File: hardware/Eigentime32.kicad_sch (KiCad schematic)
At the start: 0 parts

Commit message: Add Power schematic sheet
CR2032 in a Keystone 3034 SMT retainer, DMG2305UX P-FET reverse
protection (gate to GND), 100 uF + 100 nF on VBAT, and a TPS61099
adjustable boost set to 3.0 V (R1 402k / R2 200k, 1 uH WE-LQS,
10 uF CIN, 2 x 10 uF COUT, 1M pull-down on EN). The sheet exposes
VBAT, VLCD and LCD_PWR_EN as hierarchical pins. ERC is clean with
all severities enabled.

Co-Authored-By: Claude Opus 5.5 (1M context) <noreply@anthropic.com>
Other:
- added sheet Power (power.kicad_sch)
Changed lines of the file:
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@@
 	(generator_version "9.0")
 	(paper "A4")
-	(title_block
-		(title "Eigentime32")
+	(title_block (title "Eigentime32"))
+	(sheet (at 50.8 50.8) (size 30.48 15.24) (exclude_from_sim no) (in_bom yes) (on_board yes) (dnp no)
+		(fields_autoplaced yes)
+		(stroke (width 0.1524) (type solid))
+		(fill (color 0 0 0 0.0000))
+		(property "Sheetname" "Power" (at 50.8 50.0884 0) (effects (font (size 1.27 1.27)) (justify left bottom)))
+		(property "Sheetfile" "power.kicad_sch" (at 50.8 66.6246 0) (effects (font (size 1.27 1.27)) (justify left top)))
+		(pin "VBAT" output (at 81.28 53.34 0) (effects (font (size 1.27 1.27)) (justify right)))
+		(pin "VLCD" output (at 81.28 55.88 0) (effects (font (size 1.27 1.27)) (justify right)))
+		(pin "LCD_PWR_EN" input (at 81.28 58.42 0) (effects (font (size 1.27 1.27)) (justify right)))
+		(instances (project "Eigentime32" (path "/6b2f6c1e-3a0d-4e6b-9a51-0e5c2f3d7a10" (page "2"))))
 	)
-	(sheet_instances
-		(path "/"
-			(page "1")
-		)
-	)
+	(wire (pts (xy 81.28 53.34) (xy 88.9 53.34)) (stroke (width 0) (type default)))
+	(label "VBAT" (at 88.9 53.34 0) (effects (font (size 1.27 1.27)) (justify left bottom)))
+	(wire (pts (xy 81.28 55.88) (xy 88.9 55.88)) (stroke (width 0) (type default)))
+	(label "VLCD" (at 88.9 55.88 0) (effects (font (size 1.27 1.27)) (justify left bottom)))
+	(wire (pts (xy 81.28 58.42) (xy 88.9 58.42)) (stroke (width 0) (type default)))
+	(label "LCD_PWR_EN" (at 88.9 58.42 0) (effects (font (size 1.27 1.27)) (justify left bottom)))
+	(sheet_instances (path "/" (page "1")))
 	(embedded_fonts no)
 )

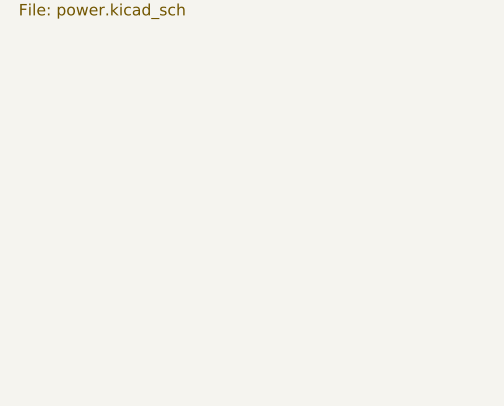
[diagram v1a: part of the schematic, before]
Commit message: Add RTC schematic sheet
RV-3032-C7 (project symbol, RV-3032 pinout) on always-on VBAT with
100 nF decoupling, 10k I2C pull-ups, 470k INT pull-up, EVI tied high
and a CLKOUT test pad. VBAT, SDA, SCL, RTC_INT and RTC_CLKOUT are
hierarchical pins.

No VBACKUP bridge: the pin is tied to VSS through 10k with switchover
off (BSM = 00). An MLCC's IR spec (50 MOhm.uF, i.e. a 50 s
self-discharge time constant) can't guarantee a 60 s cell swap at any
size, and its worst-case leakage would exceed the ~1 uA budget. C1 is
removed from the BOM. ERC is clean with all severities enabled.

Co-Authored-By: Claude Opus 5.5 (1M context) <noreply@anthropic.com>
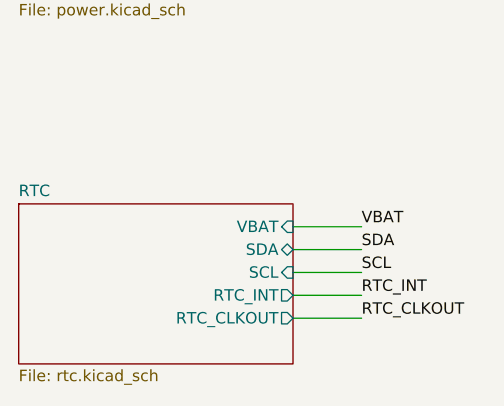
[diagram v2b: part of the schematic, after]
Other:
- added sheet RTC (rtc.kicad_sch)
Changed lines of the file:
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@@
 		(instances (project "Eigentime32" (path "/6b2f6c1e-3a0d-4e6b-9a51-0e5c2f3d7a10" (page "2"))))
+	)
+	(sheet (at 50.8 88.9) (size 30.48 17.78) (exclude_from_sim no) (in_bom yes) (on_board yes) (dnp no)
+		(fields_autoplaced yes)
+		(stroke (width 0.1524) (type solid))
+		(fill (color 0 0 0 0.0000))
+		(property "Sheetname" "RTC" (at 50.8 88.1884 0) (effects (font (size 1.27 1.27)) (justify left bottom)))
+		(property "Sheetfile" "rtc.kicad_sch" (at 50.8 107.2646 0) (effects (font (size 1.27 1.27)) (justify left top)))
+		(pin "VBAT" input (at 81.28 91.44 0) (effects (font (size 1.27 1.27)) (justify right)))
+		(pin "SDA" bidirectional (at 81.28 93.98 0) (effects (font (size 1.27 1.27)) (justify right)))
+		(pin "SCL" input (at 81.28 96.52 0) (effects (font (size 1.27 1.27)) (justify right)))
+		(pin "RTC_INT" output (at 81.28 99.06 0) (effects (font (size 1.27 1.27)) (justify right)))
+		(pin "RTC_CLKOUT" output (at 81.28 101.6 0) (effects (font (size 1.27 1.27)) (justify right)))
+		(instances (project "Eigentime32" (path "/6b2f6c1e-3a0d-4e6b-9a51-0e5c2f3d7a10" (page "3"))))
 	)
 	(wire (pts (xy 81.28 53.34) (xy 88.9 53.34)) (stroke (width 0) (type default)))
@@
 	(wire (pts (xy 81.28 58.42) (xy 88.9 58.42)) (stroke (width 0) (type default)))
 	(label "LCD_PWR_EN" (at 88.9 58.42 0) (effects (font (size 1.27 1.27)) (justify left bottom)))
+	(wire (pts (xy 81.28 91.44) (xy 88.9 91.44)) (stroke (width 0) (type default)))
+	(label "VBAT" (at 88.9 91.44 0) (effects (font (size 1.27 1.27)) (justify left bottom)))
+	(wire (pts (xy 81.28 93.98) (xy 88.9 93.98)) (stroke (width 0) (type default)))
+	(label "SDA" (at 88.9 93.98 0) (effects (font (size 1.27 1.27)) (justify left bottom)))
+	(wire (pts (xy 81.28 96.52) (xy 88.9 96.52)) (stroke (width 0) (type default)))
+	(label "SCL" (at 88.9 96.52 0) (effects (font (size 1.27 1.27)) (justify left bottom)))
+	(wire (pts (xy 81.28 99.06) (xy 88.9 99.06)) (stroke (width 0) (type default)))
+	(label "RTC_INT" (at 88.9 99.06 0) (effects (font (size 1.27 1.27)) (justify left bottom)))
+	(wire (pts (xy 81.28 101.6) (xy 88.9 101.6)) (stroke (width 0) (type default)))
+	(label "RTC_CLKOUT" (at 88.9 101.6 0) (effects (font (size 1.27 1.27)) (justify left bottom)))
 	(sheet_instances (path "/" (page "1")))
 	(embedded_fonts no)

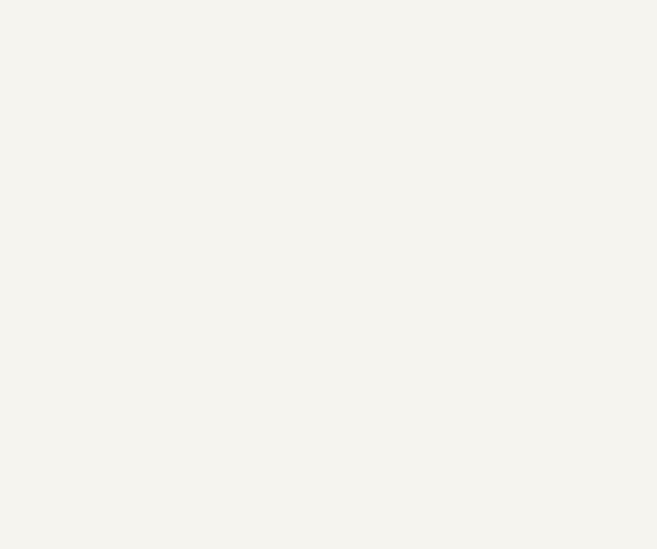
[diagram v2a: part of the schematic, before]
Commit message: Add MCU sheet and update design docs
STM32L031G6U6 (UFQFPN28) on VBAT with ST's decoupling (10 uF bulk
fitted as DNP because of IR leakage), NRST filter, BOOT0 pull-down,
TC2030-NL SWD pads, NC lid reed switch and two buttons with 1M
external pull-ups. Wake sources sit on distinct EXTI lines; SPI1 on
PA5/PA7 and I2C1 on PB6/PB7. LCD and NFC sheet pins are marked
no-connect at the root until those sheets exist.

Docs now match the schematics: load switch, inrush resistor, boost EN
delay, LCD buffer requirement, Keystone 3034 height (~8.4 mm total),
backup bridge dropped pending Alex, and the MCU pin map.

ERC is clean with all severities enabled.

Co-Authored-By: Claude Opus 5.5 (1M context) <noreply@anthropic.com>
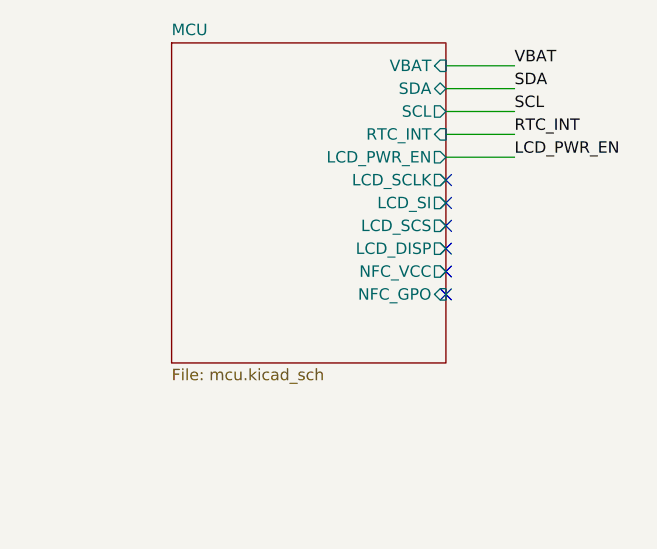
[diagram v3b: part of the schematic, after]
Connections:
- no-connect marks 0 -> 6
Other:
- added sheet MCU (mcu.kicad_sch)
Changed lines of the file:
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@@
 		(instances (project "Eigentime32" (path "/6b2f6c1e-3a0d-4e6b-9a51-0e5c2f3d7a10" (page "3"))))
+	)
+	(sheet (at 121.92 50.8) (size 30.48 35.56) (exclude_from_sim no) (in_bom yes) (on_board yes) (dnp no)
+		(fields_autoplaced yes)
+		(stroke (width 0.1524) (type solid))
+		(fill (color 0 0 0 0.0000))
+		(property "Sheetname" "MCU" (at 121.92 50.0884 0) (effects (font (size 1.27 1.27)) (justify left bottom)))
+		(property "Sheetfile" "mcu.kicad_sch" (at 121.92 86.9446 0) (effects (font (size 1.27 1.27)) (justify left top)))
+		(pin "VBAT" input (at 152.4 53.34 0) (effects (font (size 1.27 1.27)) (justify right)))
+		(pin "SDA" bidirectional (at 152.4 55.88 0) (effects (font (size 1.27 1.27)) (justify right)))
+		(pin "SCL" output (at 152.4 58.42 0) (effects (font (size 1.27 1.27)) (justify right)))
+		(pin "RTC_INT" input (at 152.4 60.96 0) (effects (font (size 1.27 1.27)) (justify right)))
+		(pin "LCD_PWR_EN" output (at 152.4 63.5 0) (effects (font (size 1.27 1.27)) (justify right)))
+		(pin "LCD_SCLK" output (at 152.4 66.04 0) (effects (font (size 1.27 1.27)) (justify right)))
+		(pin "LCD_SI" output (at 152.4 68.58 0) (effects (font (size 1.27 1.27)) (justify right)))
+		(pin "LCD_SCS" output (at 152.4 71.12 0) (effects (font (size 1.27 1.27)) (justify right)))
+		(pin "LCD_DISP" output (at 152.4 73.66 0) (effects (font (size 1.27 1.27)) (justify right)))
+		(pin "NFC_VCC" output (at 152.4 76.2 0) (effects (font (size 1.27 1.27)) (justify right)))
+		(pin "NFC_GPO" input (at 152.4 78.74 0) (effects (font (size 1.27 1.27)) (justify right)))
+		(instances (project "Eigentime32" (path "/6b2f6c1e-3a0d-4e6b-9a51-0e5c2f3d7a10" (page "4"))))
 	)
 	(wire (pts (xy 81.28 53.34) (xy 88.9 53.34)) (stroke (width 0) (type default)))
@@
 	(wire (pts (xy 81.28 101.6) (xy 88.9 101.6)) (stroke (width 0) (type default)))
 	(label "RTC_CLKOUT" (at 88.9 101.6 0) (effects (font (size 1.27 1.27)) (justify left bottom)))
+	(wire (pts (xy 152.4 53.34) (xy 160.02 53.34)) (stroke (width 0) (type default)))
+	(label "VBAT" (at 160.02 53.34 0) (effects (font (size 1.27 1.27)) (justify left bottom)))
+	(wire (pts (xy 152.4 55.88) (xy 160.02 55.88)) (stroke (width 0) (type default)))
+	(label "SDA" (at 160.02 55.88 0) (effects (font (size 1.27 1.27)) (justify left bottom)))
+	(wire (pts (xy 152.4 58.42) (xy 160.02 58.42)) (stroke (width 0) (type default)))
+	(label "SCL" (at 160.02 58.42 0) (effects (font (size 1.27 1.27)) (justify left bottom)))
+	(wire (pts (xy 152.4 60.96) (xy 160.02 60.96)) (stroke (width 0) (type default)))
+	(label "RTC_INT" (at 160.02 60.96 0) (effects (font (size 1.27 1.27)) (justify left bottom)))
+	(wire (pts (xy 152.4 63.5) (xy 160.02 63.5)) (stroke (width 0) (type default)))
+	(label "LCD_PWR_EN" (at 160.02 63.5 0) (effects (font (size 1.27 1.27)) (justify left bottom)))
+	(no_connect (at 152.4 66.04))
+	(no_connect (at 152.4 68.58))
+	(no_connect (at 152.4 71.12))
+	(no_connect (at 152.4 73.66))
+	(no_connect (at 152.4 76.2))
+	(no_connect (at 152.4 78.74))
 	(sheet_instances (path "/" (page "1")))
 	(embedded_fonts no)

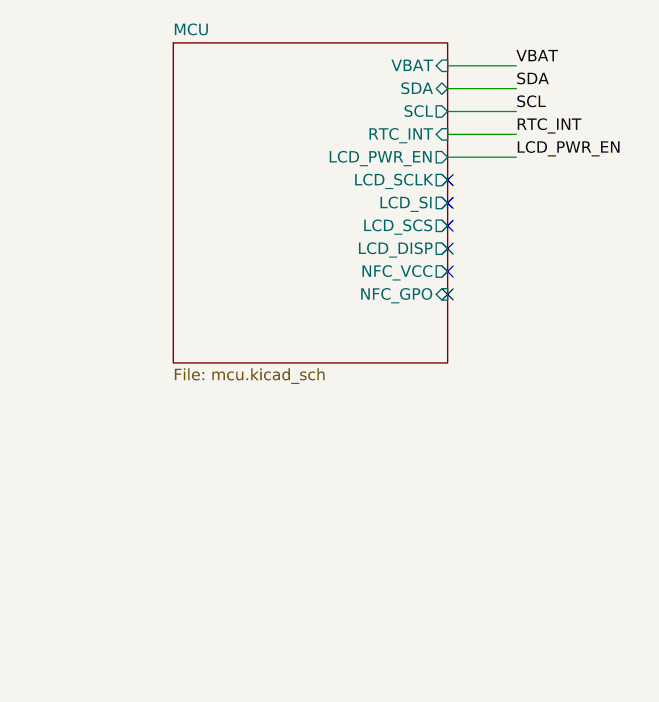
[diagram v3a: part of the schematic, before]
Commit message: Add LCD sheet; mark backup-bridge drop as confirmed
LS013B7DH03 on a Panasonic AYF531035 FPC connector (Sharp's
recommended part: 0.5 mm, 10 pin, back lock, 1.0 mm high, top and
bottom contact), with a project footprint from Panasonic's land
pattern. Decoupling per Sharp Figure 9-1: 1 uF on VDD and VDDA,
0.1 uF on DISP. EXTMODE is tied to VLCD for external EXTCOMIN.

SCLK/SI/SCS/DISP go through an SN74LV4T125 and EXTCOMIN (RTC CLKOUT)
through an SN74LV1T34, both powered from VLCD. VIH is 1.35-1.39 V
max at VCC 3.0-3.6 V, so VBAT-level inputs down to ~2.0 V translate;
the LV4T125 has Ioff. The root-sheet no-connects for the LCD lines
are removed; only NFC_VCC/NFC_GPO remain.

Docs: the RTC backup bridge drop is confirmed by Alex (2026-10-10).
ERC is clean with all severities enabled.

Co-Authored-By: Claude Opus 5.5 (1M context) <noreply@anthropic.com>
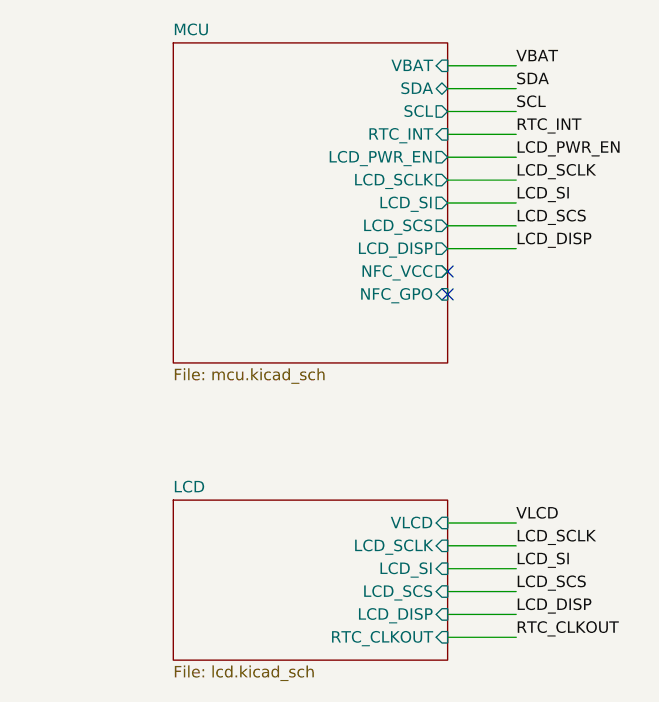
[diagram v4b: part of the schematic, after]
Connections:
- no-connect marks 6 -> 2
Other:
- added sheet LCD (lcd.kicad_sch)
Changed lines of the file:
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@@
 		(instances (project "Eigentime32" (path "/6b2f6c1e-3a0d-4e6b-9a51-0e5c2f3d7a10" (page "4"))))
+	)
+	(sheet (at 121.92 101.6) (size 30.48 17.78) (exclude_from_sim no) (in_bom yes) (on_board yes) (dnp no)
+		(fields_autoplaced yes)
+		(stroke (width 0.1524) (type solid))
+		(fill (color 0 0 0 0.0000))
+		(property "Sheetname" "LCD" (at 121.92 100.8884 0) (effects (font (size 1.27 1.27)) (justify left bottom)))
+		(property "Sheetfile" "lcd.kicad_sch" (at 121.92 119.9646 0) (effects (font (size 1.27 1.27)) (justify left top)))
+		(pin "VLCD" input (at 152.4 104.14 0) (effects (font (size 1.27 1.27)) (justify right)))
+		(pin "LCD_SCLK" input (at 152.4 106.68 0) (effects (font (size 1.27 1.27)) (justify right)))
+		(pin "LCD_SI" input (at 152.4 109.22 0) (effects (font (size 1.27 1.27)) (justify right)))
+		(pin "LCD_SCS" input (at 152.4 111.76 0) (effects (font (size 1.27 1.27)) (justify right)))
+		(pin "LCD_DISP" input (at 152.4 114.3 0) (effects (font (size 1.27 1.27)) (justify right)))
+		(pin "RTC_CLKOUT" input (at 152.4 116.84 0) (effects (font (size 1.27 1.27)) (justify right)))
+		(instances (project "Eigentime32" (path "/6b2f6c1e-3a0d-4e6b-9a51-0e5c2f3d7a10" (page "5"))))
 	)
 	(wire (pts (xy 81.28 53.34) (xy 88.9 53.34)) (stroke (width 0) (type default)))
@@
 	(wire (pts (xy 152.4 63.5) (xy 160.02 63.5)) (stroke (width 0) (type default)))
 	(label "LCD_PWR_EN" (at 160.02 63.5 0) (effects (font (size 1.27 1.27)) (justify left bottom)))
-	(no_connect (at 152.4 66.04))
-	(no_connect (at 152.4 68.58))
-	(no_connect (at 152.4 71.12))
-	(no_connect (at 152.4 73.66))
+	(wire (pts (xy 152.4 66.04) (xy 160.02 66.04)) (stroke (width 0) (type default)))
+	(label "LCD_SCLK" (at 160.02 66.04 0) (effects (font (size 1.27 1.27)) (justify left bottom)))
+	(wire (pts (xy 152.4 68.58) (xy 160.02 68.58)) (stroke (width 0) (type default)))
+	(label "LCD_SI" (at 160.02 68.58 0) (effects (font (size 1.27 1.27)) (justify left bottom)))
+	(wire (pts (xy 152.4 71.12) (xy 160.02 71.12)) (stroke (width 0) (type default)))
+	(label "LCD_SCS" (at 160.02 71.12 0) (effects (font (size 1.27 1.27)) (justify left bottom)))
+	(wire (pts (xy 152.4 73.66) (xy 160.02 73.66)) (stroke (width 0) (type default)))
+	(label "LCD_DISP" (at 160.02 73.66 0) (effects (font (size 1.27 1.27)) (justify left bottom)))
 	(no_connect (at 152.4 76.2))
 	(no_connect (at 152.4 78.74))
+	(wire (pts (xy 152.4 104.14) (xy 160.02 104.14)) (stroke (width 0) (type default)))
+	(label "VLCD" (at 160.02 104.14 0) (effects (font (size 1.27 1.27)) (justify left bottom)))
+	(wire (pts (xy 152.4 106.68) (xy 160.02 106.68)) (stroke (width 0) (type default)))
+	(label "LCD_SCLK" (at 160.02 106.68 0) (effects (font (size 1.27 1.27)) (justify left bottom)))
+	(wire (pts (xy 152.4 109.22) (xy 160.02 109.22)) (stroke (width 0) (type default)))
+	(label "LCD_SI" (at 160.02 109.22 0) (effects (font (size 1.27 1.27)) (justify left bottom)))
+	(wire (pts (xy 152.4 111.76) (xy 160.02 111.76)) (stroke (width 0) (type default)))
+	(label "LCD_SCS" (at 160.02 111.76 0) (effects (font (size 1.27 1.27)) (justify left bottom)))
+	(wire (pts (xy 152.4 114.3) (xy 160.02 114.3)) (stroke (width 0) (type default)))
+	(label "LCD_DISP" (at 160.02 114.3 0) (effects (font (size 1.27 1.27)) (justify left bottom)))
+	(wire (pts (xy 152.4 116.84) (xy 160.02 116.84)) (stroke (width 0) (type default)))
+	(label "RTC_CLKOUT" (at 160.02 116.84 0) (effects (font (size 1.27 1.27)) (justify left bottom)))
 	(sheet_instances (path "/" (page "1")))
 	(embedded_fonts no)
